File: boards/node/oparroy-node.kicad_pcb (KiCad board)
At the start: 2 copper layers, 35 parts, among them J1 Conn_02x05_Odd_Even, J2 Conn_02x05_Odd_Even, U1 DNP, U2 SN74LVC1G3157, U3 CH32V003F4P6

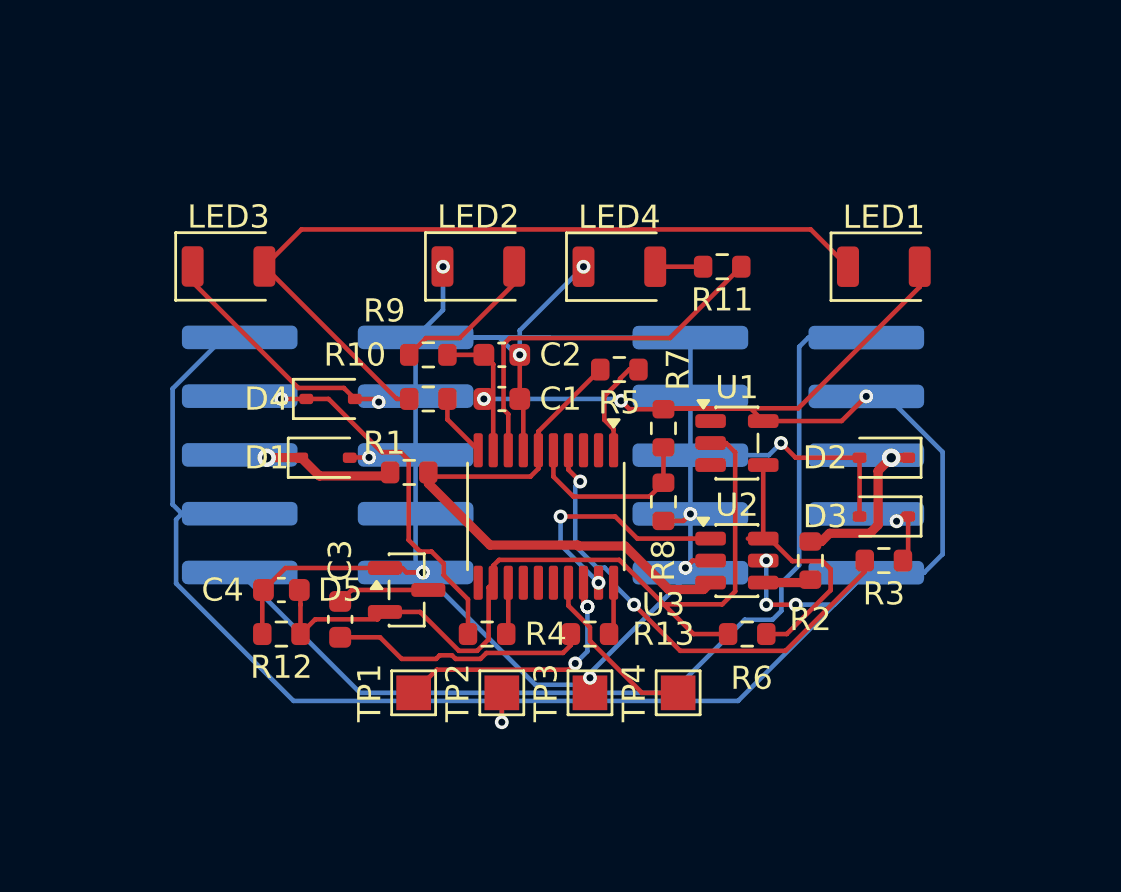
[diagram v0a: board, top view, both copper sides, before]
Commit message: boards: node layout — rounded outline, mounting holes, GND pours
The manual pcbnew pass on top of the seeded skeleton: rounded edge
cuts, 2x M2.5 mounting holes, GND pours both sides, duplicate-via and
silkscreen cleanup. The project file moves in step with the DSL
constraint decisions: opa_p out of the Bypass netclass assignments and
min_hole_clearance at 0.15 mm, spliced by hand (re-emitting
design/node_board.py would clobber the live board — the T29 hazard).

Headless DRC (kicad-cli pcb drc): 36 -> 14 violations, all intrinsic:
8x copper_edge_clearance on the LED light-pipe NPTHs (the 0.3 mm edge
floor also judges holes; pending exclusions or a footprint/quote
decision), 2x npth_inside_courtyard local overrides, 4 silkscreen
warnings.
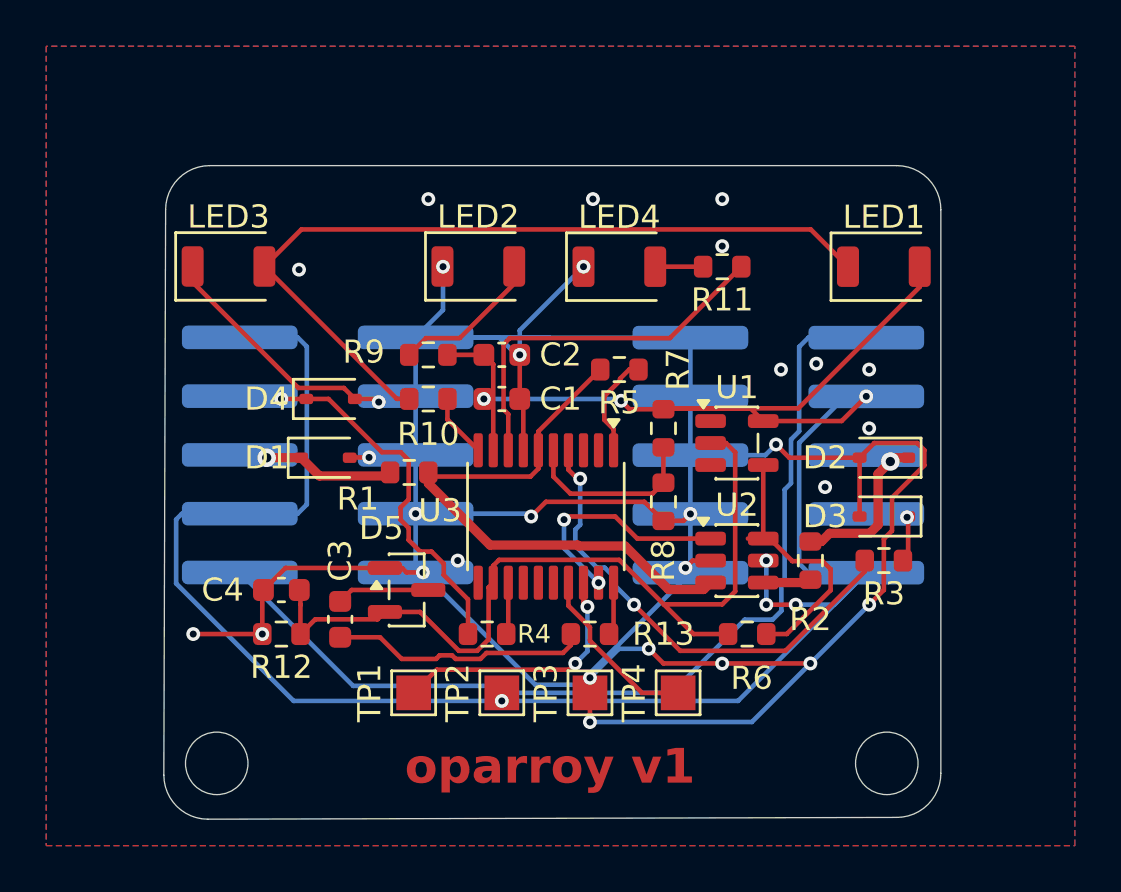
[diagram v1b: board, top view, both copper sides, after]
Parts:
- added REF**: MountingHole_2.7mm_M2.5, MountingHole:MountingHole_2.7mm_M2.5, F.Cu at (102.6, 94.5)
- added REF**: MountingHole_2.7mm_M2.5, MountingHole:MountingHole_2.7mm_M2.5, F.Cu at (131.6, 94.5)
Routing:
- net GND: track 103.1 -> 154.7 mm, vias 11 -> 30
- net 3V3: track 108.0 -> 110.1 mm
- net RX_B: track 4.44 -> 3.92 mm
- net swio: vias 3 -> 2
- added copper zone on B.Cu, net GND
- added copper zone on F.Cu, net GND
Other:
- board outline added: 33.6 x 28.2 mm
- board text added: "oparroy v1"
- board text added: "power"
- board text added: "status"

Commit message: boards: node — LED light-pipe slots shrink to 1.5x2.4 mm
Rebind LED1-LED4 to Oparroy:LED_1206_3216Metric_ReverseMount_Hole1.5x2.4mm
and narrow their embedded NPTH pads in place — positions, rotations,
uuids, tstamps, and pad nets untouched, so the back-annotation join
keys still hold. Add boards/node/fp-lib-table so pcbnew resolves the
project library in the GUI. DRC: the 8 LED copper_edge_clearance
errors are gone; every other violation is byte-identical to the
pre-change report.
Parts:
- LED1, LED2, LED3, LED4: footprint LED_SMD:LED_1206_3216Metric_ReverseMount_Hole1.8x2.4mm -> Oparroy:LED_1206_3216Metric_ReverseMount_Hole1.5x2.4mm
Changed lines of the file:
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@@
 		)
 	)
-	(footprint "LED_SMD:LED_1206_3216Metric_ReverseMount_Hole1.8x2.4mm"
+	(footprint "Oparroy:LED_1206_3216Metric_ReverseMount_Hole1.5x2.4mm"
 		(layer "F.Cu")
 		(at 113.920208 73.014686)
@@
 		(pad "" np_thru_hole oval
 			(at 0 0)
-			(size 1.8 2.4)
-			(drill oval 1.8 2.4)
+			(size 1.5 2.4)
+			(drill oval 1.5 2.4)
 			(layers "*.Cu" "*.Mask")
 		)
@@
 		)
 	)
-	(footprint "LED_SMD:LED_1206_3216Metric_ReverseMount_Hole1.8x2.4mm"
+	(footprint "Oparroy:LED_1206_3216Metric_ReverseMount_Hole1.5x2.4mm"
 		(layer "F.Cu")
 		(at 131.445 73.025)
@@
 		(pad "" np_thru_hole oval
 			(at 0 0)
-			(size 1.8 2.4)
-			(drill oval 1.8 2.4)
+			(size 1.5 2.4)
+			(drill oval 1.5 2.4)
 			(layers "*.Cu" "*.Mask")
 		)
@@
 		)
 	)
-	(footprint "LED_SMD:LED_1206_3216Metric_ReverseMount_Hole1.8x2.4mm"
+	(footprint "Oparroy:LED_1206_3216Metric_ReverseMount_Hole1.5x2.4mm"
 		(layer "F.Cu")
 		(at 103.125208 73.014686)
@@
 		(pad "" np_thru_hole oval
 			(at 0 0)
-			(size 1.8 2.4)
-			(drill oval 1.8 2.4)
+			(size 1.5 2.4)
+			(drill oval 1.5 2.4)
 			(layers "*.Cu" "*.Mask")
 		)
@@
 		(embedded_fonts no)
 	)
-	(footprint "LED_SMD:LED_1206_3216Metric_ReverseMount_Hole1.8x2.4mm"
+	(footprint "Oparroy:LED_1206_3216Metric_ReverseMount_Hole1.5x2.4mm"
 		(layer "F.Cu")
 		(at 120.015 73.025)
@@
 		(pad "" np_thru_hole oval
 			(at 0 0)
-			(size 1.8 2.4)
-			(drill oval 1.8 2.4)
+			(size 1.5 2.4)
+			(drill oval 1.5 2.4)
 			(layers "*.Cu" "*.Mask")
 		)
